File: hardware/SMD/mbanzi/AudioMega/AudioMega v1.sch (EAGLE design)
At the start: 75 parts, among them Q1 BC846ASMD, Q2 BC846ASMD, Q3 BC846ASMD, Q4 2N7002, Q5 BC846ASMD, Q6 BC846ASMD, U1 REG1117-5, U2 REG1117-3.3, U3 ATMEGA328-AU, U4 LM386M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

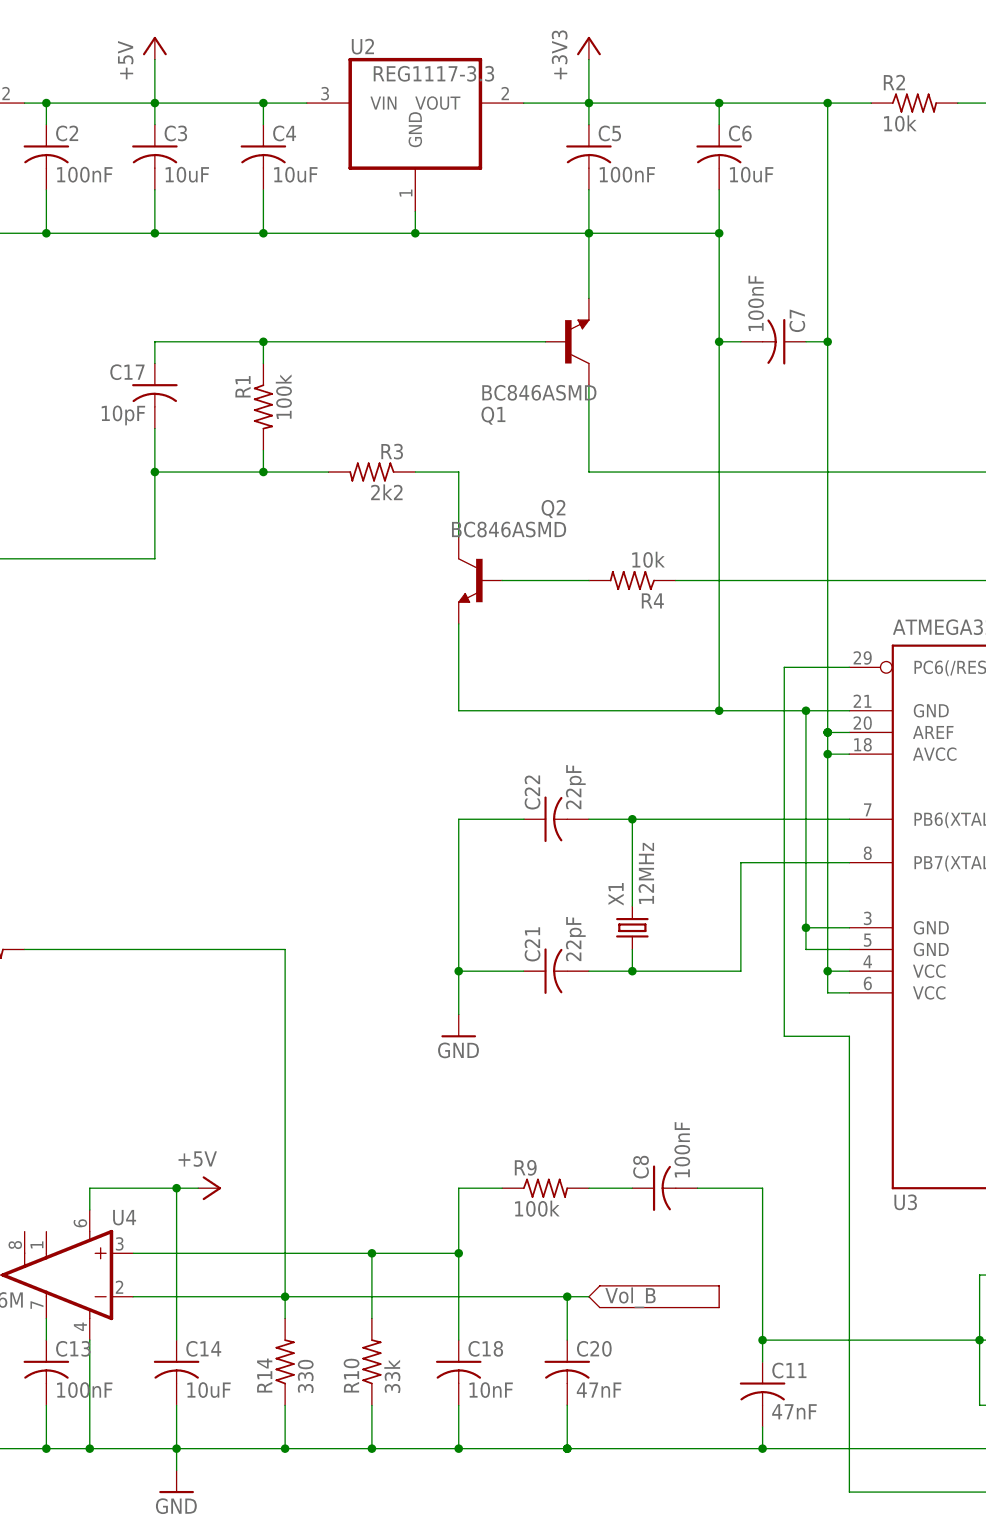
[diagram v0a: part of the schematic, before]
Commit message: Updated: - Beeper connected to M64 (base of beeper transistor) - R10 changed to 33k - deleted some capasitors
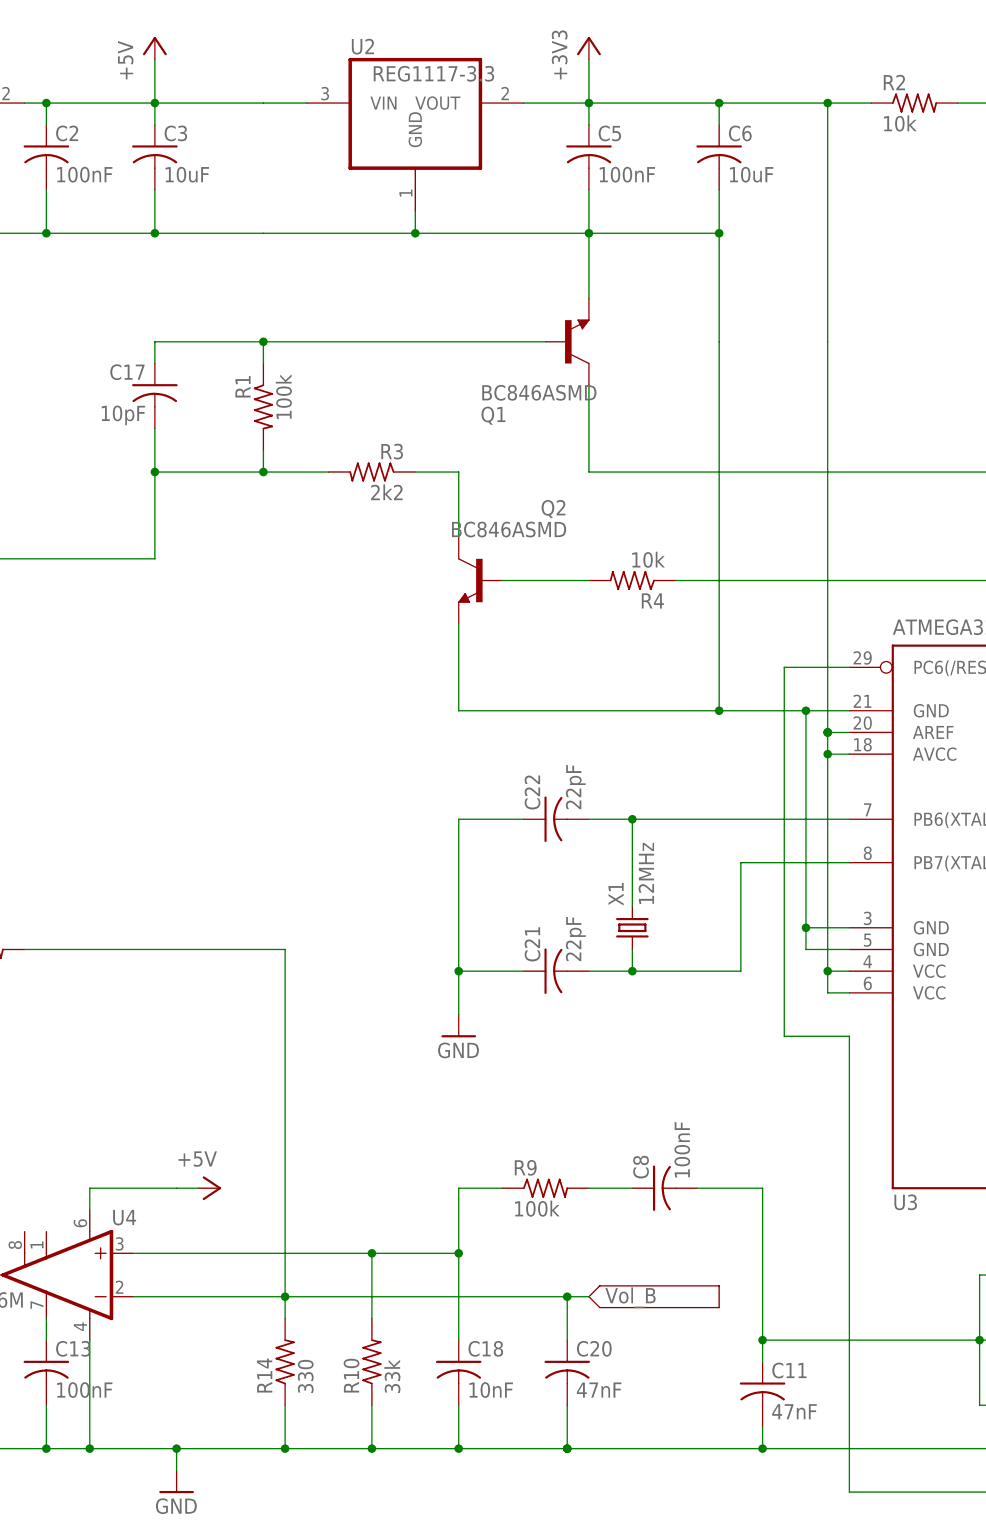
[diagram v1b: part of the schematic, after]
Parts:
- removed C14, C4: 10uF, resistor:C-USC1206
- removed C7: 100nF, resistor:C-USC1206
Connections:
- net +3V3: no longer C7.1
- net +5V: no longer C14.1, C4.1
- net GND: no longer C14.2, C4.2, C7.2
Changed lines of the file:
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@@
 <part name="C2" library="resistor" deviceset="C-US" device="C1206" value="100nF"/>
 <part name="C3" library="resistor" deviceset="C-US" device="C1206" value="10uF"/>
-<part name="C4" library="resistor" deviceset="C-US" device="C1206" value="10uF"/>
 <part name="C5" library="resistor" deviceset="C-US" device="C1206" value="100nF"/>
 <part name="C6" library="resistor" deviceset="C-US" device="C1206" value="10uF"/>
-<part name="C7" library="resistor" deviceset="C-US" device="C1206" value="100nF"/>
 <part name="C8" library="resistor" deviceset="C-US" device="C1206" value="100nF"/>
 <part name="C9" library="resistor" deviceset="C-US" device="C1206" value="100uF"/>
@@
 <part name="C12" library="resistor" deviceset="C-US" device="C1206" value="47nF"/>
 <part name="C13" library="resistor" deviceset="C-US" device="C1206" value="100nF"/>
-<part name="C14" library="resistor" deviceset="C-US" device="C1206" value="10uF"/>
 <part name="C15" library="resistor" deviceset="C-US" device="C1206" value="100nF"/>
 <part name="C16" library="resistor" deviceset="C-US" device="C1206" value="47uF"/>
@@
 <instance part="C2" gate="G$1" x="55.88" y="157.48"/>
 <instance part="C3" gate="G$1" x="68.58" y="157.48"/>
-<instance part="C4" gate="G$1" x="81.28" y="157.48"/>
 <instance part="C5" gate="G$1" x="119.38" y="157.48"/>
 <instance part="C6" gate="G$1" x="134.62" y="157.48"/>
-<instance part="C7" gate="G$1" x="142.24" y="134.62" rot="MR90"/>
 <instance part="C8" gate="G$1" x="127" y="35.56" rot="R90"/>
 <instance part="C9" gate="G$1" x="33.02" y="38.1" rot="R90"/>
@@
 <instance part="C12" gate="G$1" x="33.02" y="15.24" rot="R90"/>
 <instance part="C13" gate="G$1" x="55.88" y="15.24"/>
-<instance part="C14" gate="G$1" x="71.12" y="15.24"/>
 <instance part="C15" gate="G$1" x="223.52" y="12.7"/>
 <instance part="C16" gate="G$1" x="33.02" y="50.8" rot="R90"/>
@@
 <wire x1="60.96" y1="17.78" x2="60.96" y2="5.08" width="0.1524" layer="91"/>
 <junction x="60.96" y="5.08"/>
-<pinref part="C14" gate="G$1" pin="2"/>
-<wire x1="71.12" y1="10.16" x2="71.12" y2="5.08" width="0.1524" layer="91"/>
 <pinref part="C13" gate="G$1" pin="2"/>
 <wire x1="55.88" y1="10.16" x2="55.88" y2="5.08" width="0.1524" layer="91"/>
@@
 <pinref part="C3" gate="G$1" pin="2"/>
 <wire x1="68.58" y1="152.4" x2="68.58" y2="147.32" width="0.1524" layer="91"/>
-<pinref part="C4" gate="G$1" pin="2"/>
-<wire x1="81.28" y1="152.4" x2="81.28" y2="147.32" width="0.1524" layer="91"/>
 <pinref part="U2" gate="G$1" pin="GND"/>
 <wire x1="99.06" y1="149.86" x2="99.06" y2="147.32" width="0.1524" layer="91"/>
@@
 <junction x="55.88" y="147.32"/>
 <junction x="68.58" y="147.32"/>
-<junction x="81.28" y="147.32"/>
 <junction x="99.06" y="147.32"/>
 <junction x="119.38" y="147.32"/>
@@
 <wire x1="104.14" y1="91.44" x2="104.14" y2="101.6" width="0.1524" layer="91"/>
 <wire x1="134.62" y1="91.44" x2="104.14" y2="91.44" width="0.1524" layer="91"/>
-<pinref part="C7" gate="G$1" pin="2"/>
-<wire x1="137.16" y1="134.62" x2="134.62" y2="134.62" width="0.1524" layer="91"/>
-<junction x="134.62" y="134.62"/>
 <pinref part="Q1" gate="G$1" pin="E"/>
 <wire x1="119.38" y1="139.7" x2="119.38" y2="147.32" width="0.1524" layer="91"/>
@@
 <wire x1="60.96" y1="33.02" x2="60.96" y2="35.56" width="0.1524" layer="91"/>
 <wire x1="60.96" y1="35.56" x2="71.12" y2="35.56" width="0.1524" layer="91"/>
-<pinref part="C14" gate="G$1" pin="1"/>
-<wire x1="71.12" y1="17.78" x2="71.12" y2="35.56" width="0.1524" layer="91"/>
 <pinref part="P+1" gate="1" pin="+5V"/>
 <wire x1="73.66" y1="35.56" x2="71.12" y2="35.56" width="0.1524" layer="91"/>
-<junction x="71.12" y="35.56"/>
 </segment>
 <segment>
@@
 <pinref part="C3" gate="G$1" pin="1"/>
 <wire x1="68.58" y1="160.02" x2="68.58" y2="162.56" width="0.1524" layer="91"/>
-<pinref part="C4" gate="G$1" pin="1"/>
-<wire x1="81.28" y1="160.02" x2="81.28" y2="162.56" width="0.1524" layer="91"/>
 <junction x="55.88" y="162.56"/>
 <junction x="68.58" y="162.56"/>
-<junction x="81.28" y="162.56"/>
 </segment>
 <segment>
@@
 <wire x1="134.62" y1="160.02" x2="134.62" y2="162.56" width="0.1524" layer="91"/>
 <junction x="134.62" y="162.56"/>
-<pinref part="C7" gate="G$1" pin="1"/>
-<wire x1="144.78" y1="134.62" x2="147.32" y2="134.62" width="0.1524" layer="91"/>
-<junction x="147.32" y="134.62"/>
-</segment>
-<segment>
+</segment>
+<segment>

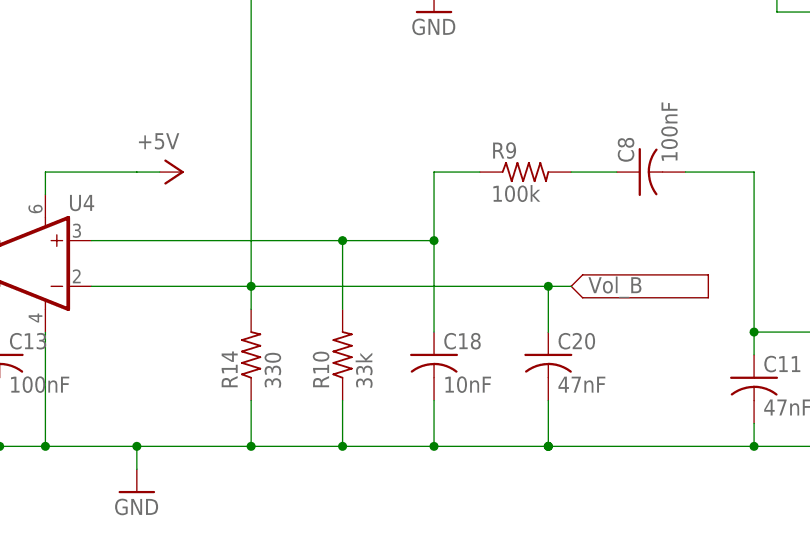
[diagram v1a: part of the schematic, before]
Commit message: Updated: Maked in corresponding of last hageha version. - changed R09, not r10, to 33k.
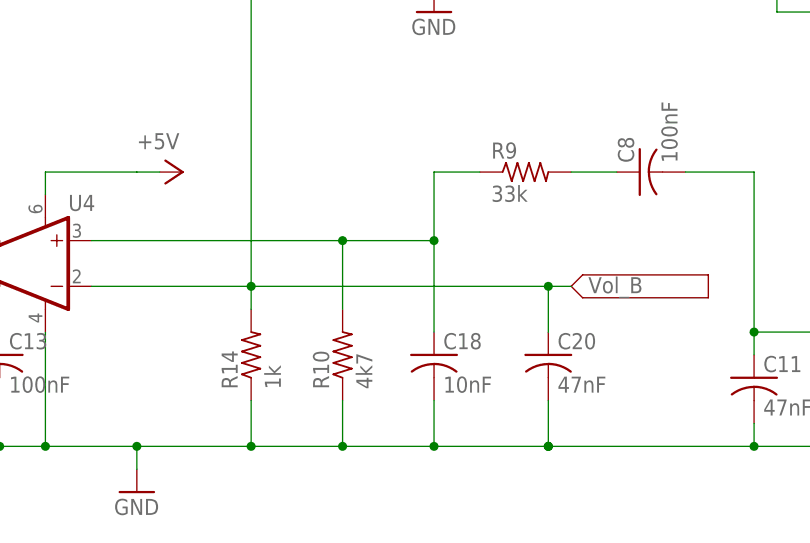
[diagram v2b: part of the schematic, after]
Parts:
- R10: value 33k -> 4k7
- R14: value 330 -> 1k
- R9: value 100k -> 33k
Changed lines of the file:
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@@
 <part name="R7" library="resistor" deviceset="R-US_" device="R1206" value="1k"/>
 <part name="R8" library="resistor" deviceset="R-US_" device="R1206" value="560k"/>
-<part name="R9" library="resistor" deviceset="R-US_" device="R1206" value="100k"/>
-<part name="R10" library="resistor" deviceset="R-US_" device="R1206" value="33k"/>
+<part name="R9" library="resistor" deviceset="R-US_" device="R1206" value="33k"/>
+<part name="R10" library="resistor" deviceset="R-US_" device="R1206" value="4k7"/>
 <part name="R11" library="resistor" deviceset="R-US_" device="R1206" value="10"/>
 <part name="R12" library="resistor" deviceset="R-US_" device="R1206" value="470k"/>
 <part name="R13" library="resistor" deviceset="R-US_" device="R1206" value="100k"/>
-<part name="R14" library="resistor" deviceset="R-US_" device="R1206" value="330"/>
+<part name="R14" library="resistor" deviceset="R-US_" device="R1206" value="1k"/>
 <part name="R15" library="resistor" deviceset="R-US_" device="R1206" value="2k2"/>
 <part name="R16" library="resistor" deviceset="R-US_" device="R1206" value="1k"/>
